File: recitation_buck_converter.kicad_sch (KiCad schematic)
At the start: 9 parts, among them U1 TPS54233

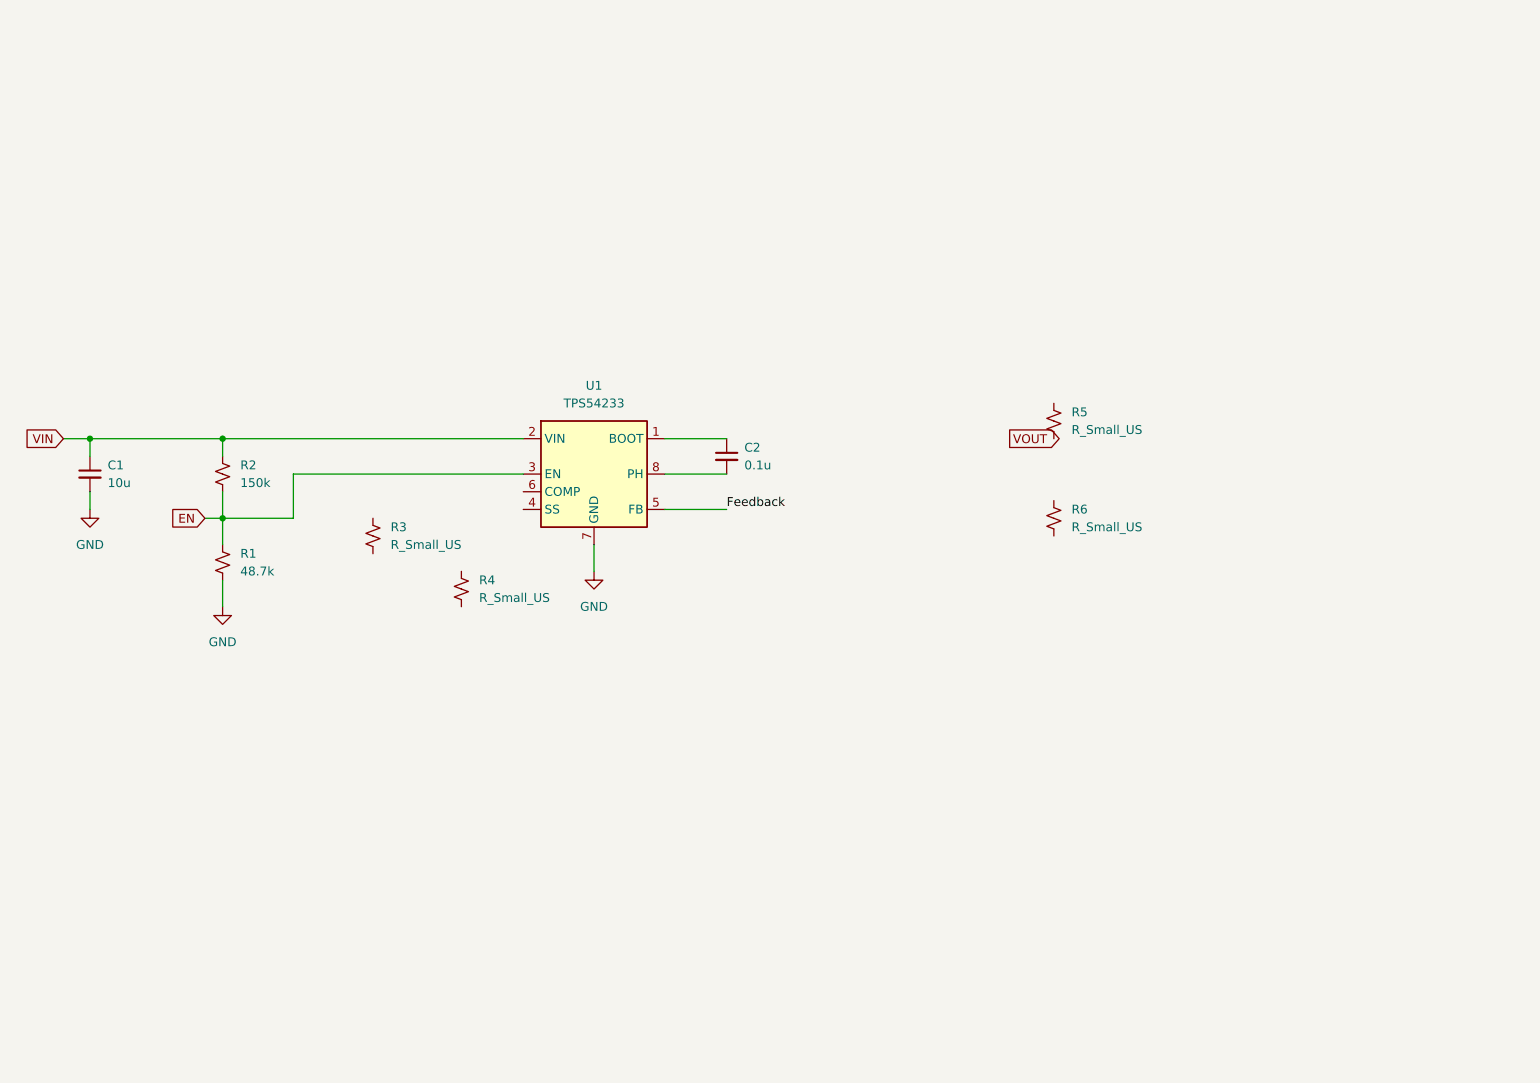
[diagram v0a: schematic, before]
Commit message: feat: update components to match specs and start layout
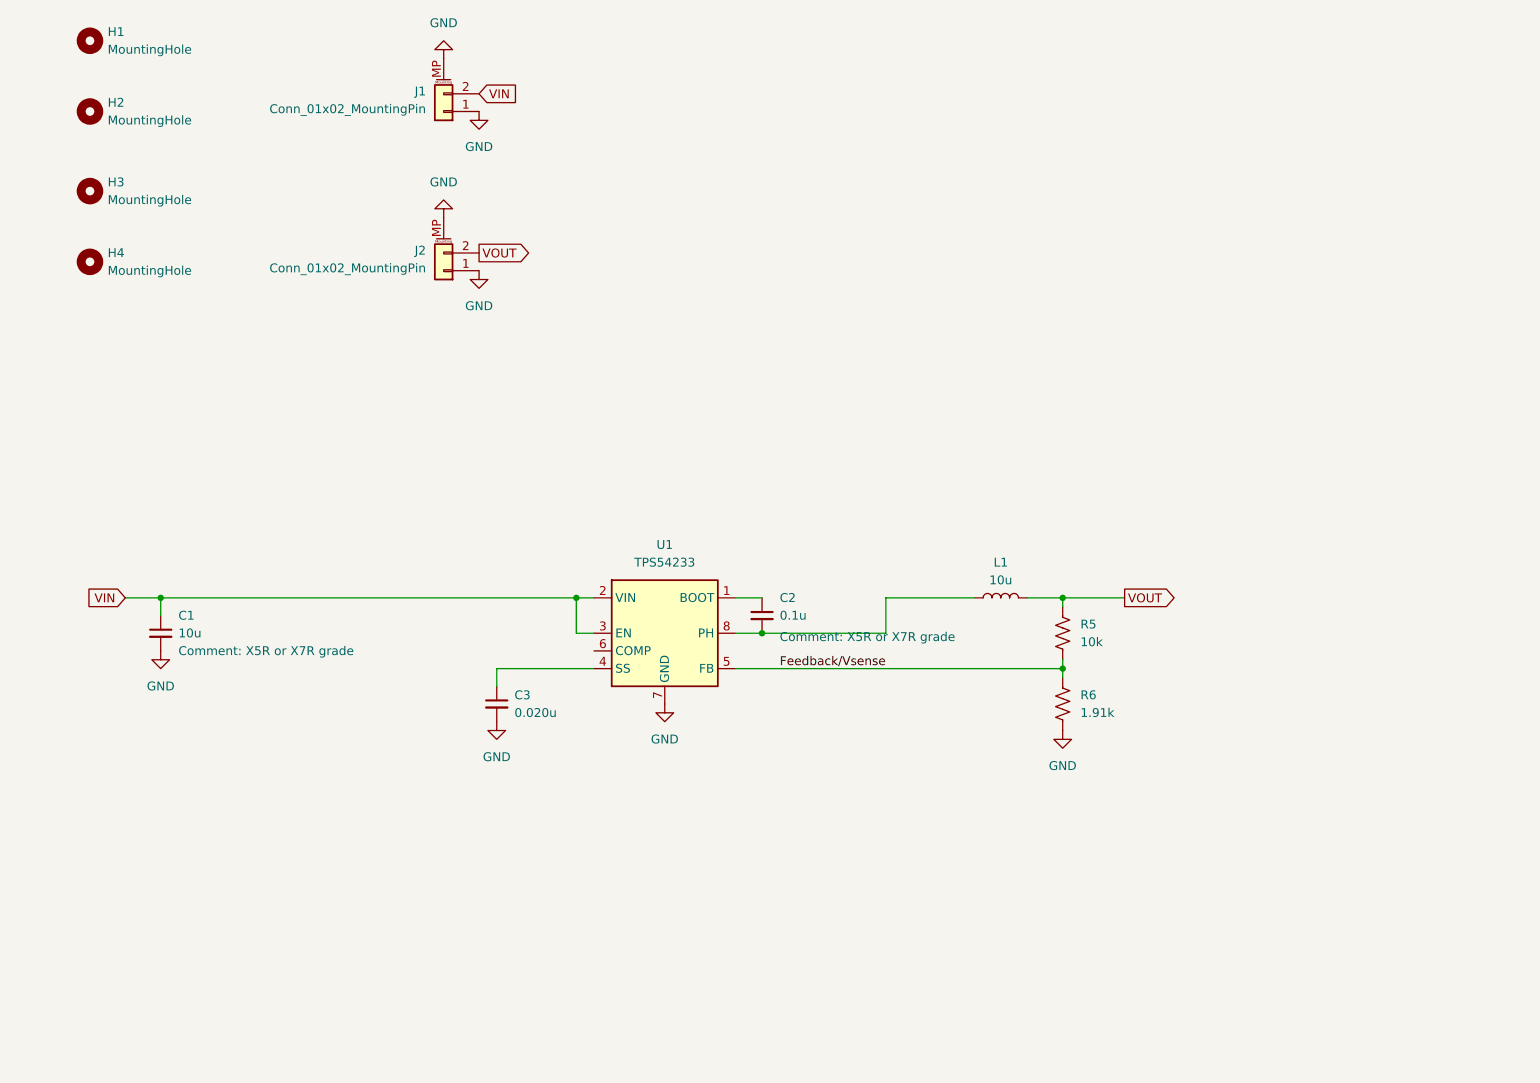
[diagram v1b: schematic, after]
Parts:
- removed R1: 48.7k, Resistor_SMD:R_0805_2012Metric_Pad1.20x1.40mm_HandSolder, symbol Device:R_Small_US
- removed R2: 150k, Resistor_SMD:R_0805_2012Metric_Pad1.20x1.40mm_HandSolder, symbol Device:R_Small_US
- removed R3, R4, R5, R6: R_Small_US, symbol Device:R_Small_US
- added C3: 0.020u, Capacitor_SMD:C_0805_2012Metric_Pad1.18x1.45mm_HandSolder, symbol Device:C_Small
- added H1, H2, H3, H4: MountingHole, MountingHole:MountingHole_2.2mm_M2, symbol Mechanical:MountingHole
- added J1, J2: Conn_01x02_MountingPin, Connector_JST:JST_XH_B2B-XH-AM_1x02_P2.50mm_Vertical, symbol Connector_Generic_MountingPin:Conn_01x02_MountingPin
- added L1: 10u, Inductor_THT:L_Axial_L9.5mm_D4.0mm_P5.08mm_Vertical_Fastron_SMCC, symbol Device:L
- added R5: 10k, Resistor_SMD:R_0805_2012Metric, symbol Device:R_US
- added R6: 1.91k, Resistor_SMD:R_0805_2012Metric, symbol Device:R_US
- C1: footprint Capacitor_SMD:C_0805_2012Metric_Pad1.18x1.45mm_HandSolder -> (none); Comment (none) -> X5R or X7R grade; Digikey PN 490-10500-1-ND -> (none)
- C2: Comment (none) -> X5R or X7R grade
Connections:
- net EN is gone; now on net VIN: U1.3 (EN)
- net GND: now also C3.2, J1.1 (Pin_1), J1.MP (MountPin), J2.1 (Pin_1), J2.MP (MountPin), R6.2
- net VIN: now also J1.2 (Pin_2)
- net VOUT: now also J2.2 (Pin_2), L1.2, R5.1
- net at U1.4 (SS): now also C3.1
- net at C2.2, U1.8 (PH): now also L1.1
- net Feedback renamed Feedback/Vsense
- net Feedback/Vsense: now also R5.2, R6.1
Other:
- moved on the sheet: C1, C2, U1

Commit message: feat: add output components, float EN, and layouu with good track width
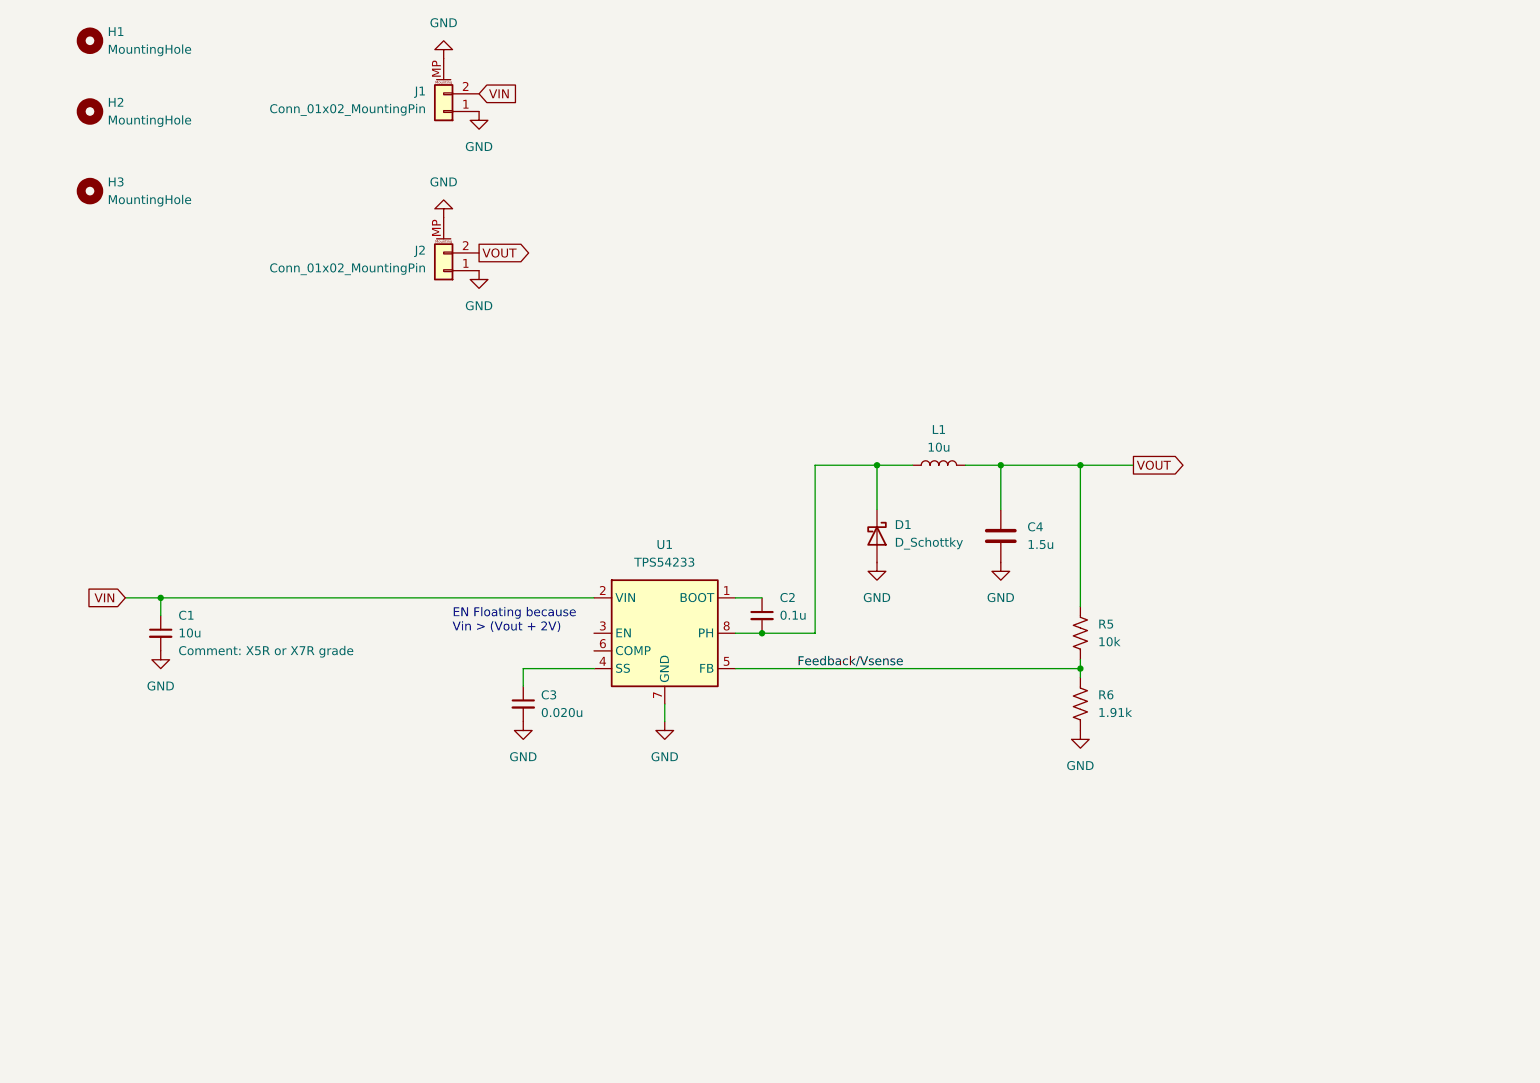
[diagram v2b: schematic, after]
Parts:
- removed H4: MountingHole, MountingHole:MountingHole_2.2mm_M2, symbol Mechanical:MountingHole
- added C4: 1.5u, Capacitor_SMD:C_0805_2012Metric_Pad1.18x1.45mm_HandSolder, symbol Device:C
- added D1: D_Schottky, ToshibaUS2H:US2H, symbol Device:D_Schottky
- C1: footprint (none) -> Capacitor_SMD:C_0805_2012Metric_Pad1.18x1.45mm_HandSolder; Digikey PN (none) -> 399-11939-2-ND
- R6: footprint Resistor_SMD:R_0805_2012Metric -> Resistor_SMD:R_0805_2012Metric_Pad1.20x1.40mm_HandSolder
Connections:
- net GND: now also C4.2, D1.2 (A)
- net VIN: no longer U1.3 (EN)
- net VOUT: now also C4.1
- net at C2.2, L1.1, U1.8 (PH): now also D1.1 (K)
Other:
- note added: "EN Floating because Vin > (Vout + 2V)"
- moved on the sheet: C3, L1, R5, R6

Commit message: feat: add compensation network; finish pcb
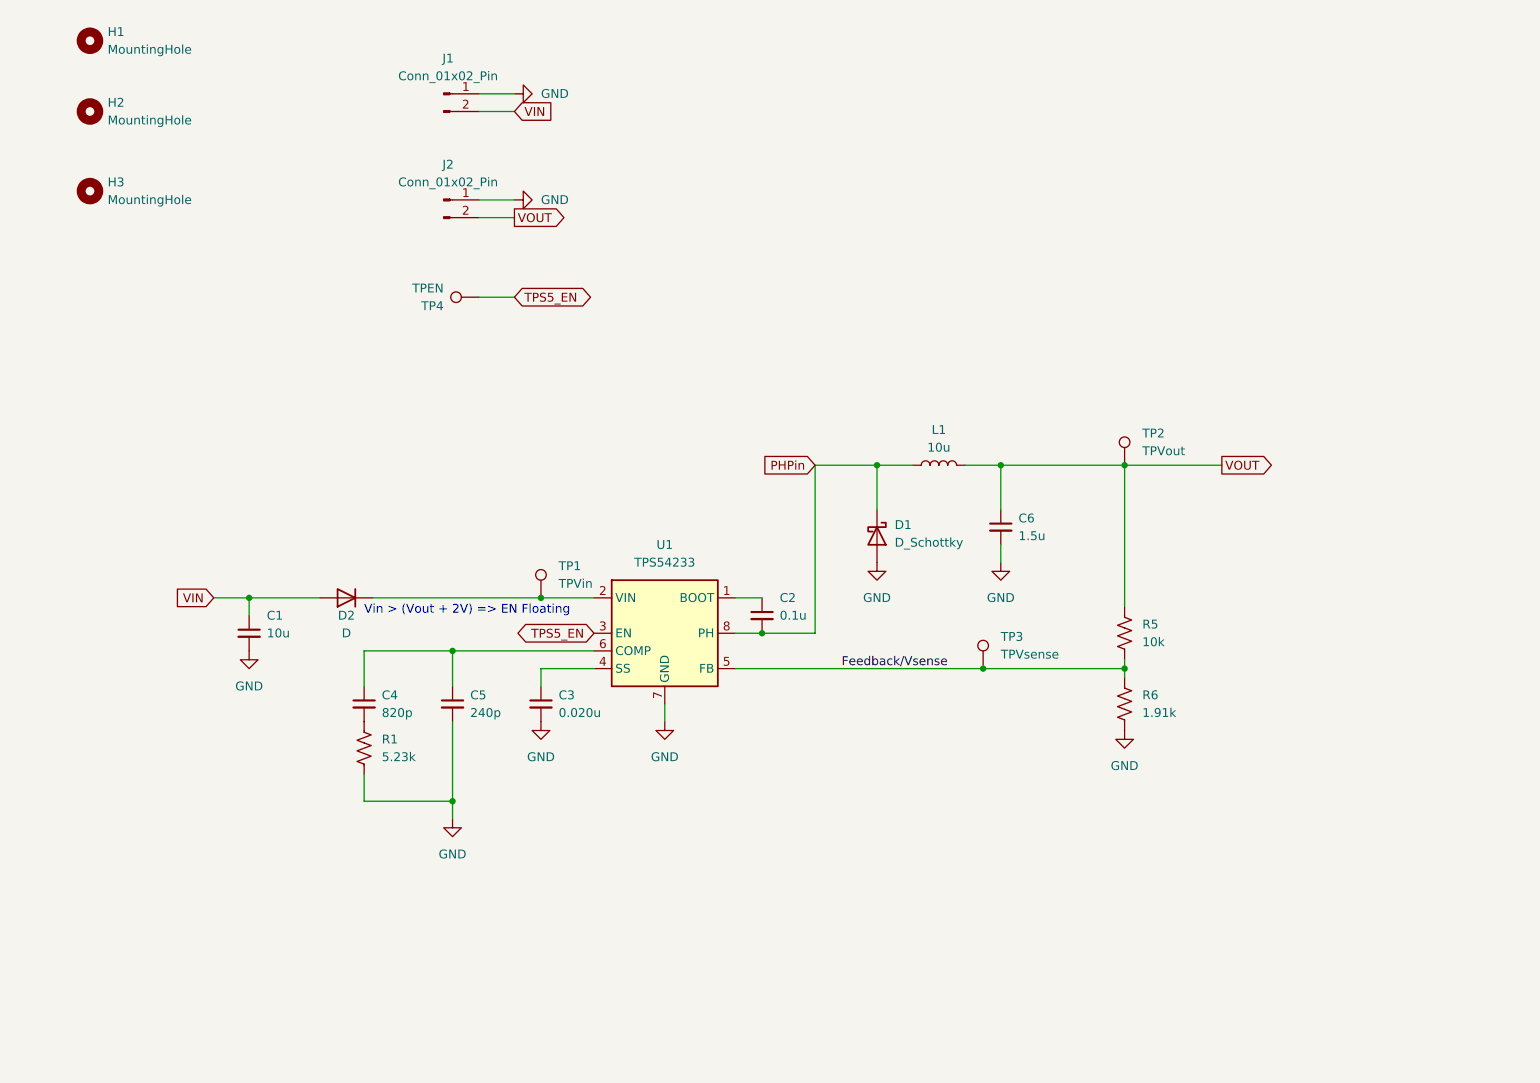
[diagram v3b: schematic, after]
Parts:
- removed C4: 1.5u, Capacitor_SMD:C_0805_2012Metric_Pad1.18x1.45mm_HandSolder, symbol Device:C
- removed J1, J2: Conn_01x02_MountingPin, Connector_JST:JST_XH_B2B-XH-AM_1x02_P2.50mm_Vertical, symbol Connector_Generic_MountingPin:Conn_01x02_MountingPin
- added C4: 820p, Capacitor_SMD:C_0805_2012Metric_Pad1.18x1.45mm_HandSolder, symbol Device:C_Small
- added C5: 240p, Capacitor_SMD:C_0805_2012Metric_Pad1.18x1.45mm_HandSolder, symbol Device:C_Small
- added C6: 1.5u, Capacitor_SMD:C_0805_2012Metric_Pad1.18x1.45mm_HandSolder, symbol Device:C_Small
- added D2: D, Diode_SMD:D_SMA, symbol Device:D
- added J1, J2: Conn_01x02_Pin, Connector_JST:JST_XH_B2B-XH-AM_1x02_P2.50mm_Vertical, symbol Connector:Conn_01x02_Pin
- added R1: 5.23k, Resistor_SMD:R_0805_2012Metric_Pad1.20x1.40mm_HandSolder, symbol Device:R_US
- added TP1: TPVin, TestPoint:TestPoint_Pad_1.5x1.5mm, symbol Connector:TestPoint
- added TP2: TPVout, TestPoint:TestPoint_Pad_1.5x1.5mm, symbol Connector:TestPoint
- added TP3: TPVsense, TestPoint:TestPoint_Pad_1.5x1.5mm, symbol Connector:TestPoint
- added TP4: TPEN, TestPoint:TestPoint_Pad_1.5x1.5mm, symbol Connector:TestPoint
- C1: Comment X5R or X7R grade -> (none)
- U1: Digikey PN 296-26985-5-ND -> 296-23902-1-ND
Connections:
- net Feedback/Vsense: now also TP3.1
- net GND: now also C5.2, C6.2, J1.1 (Pin_1), J2.1 (Pin_1), R1.2
- net VIN: now also D2.2 (A), J1.2 (Pin_2); no longer U1.2 (VIN)
- net VOUT: now also C6.1, J2.2 (Pin_2), TP2.1
- net TPS5_EN: now reaches U1.3 (EN)
- net TPS5_EN: now also TP4.1
- net at U1.6 (COMP): now also C4.1, C5.1
- net PHPin: now reaches C2.2, D1.1 (K), L1.1, U1.8 (PH)
- new net: C4.2, R1.1
- new net: D2.1 (K), TP1.1, U1.2 (VIN)
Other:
- note added: "Vin > (Vout + 2V) => EN Floating"
- note removed: "EN Floating because Vin > (Vout + 2V)"
- moved on the sheet: C1, C3, R5, R6

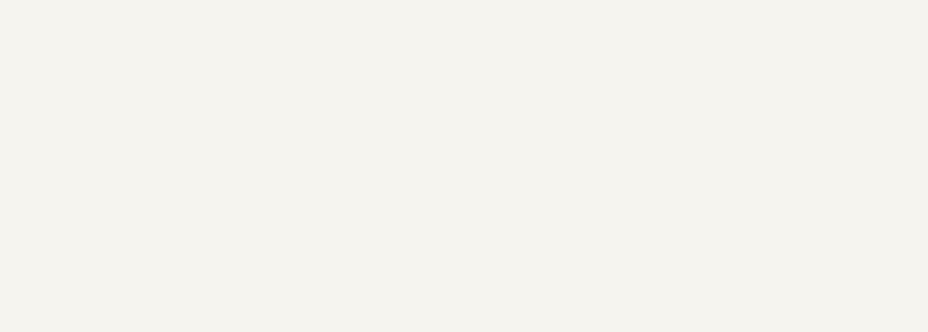
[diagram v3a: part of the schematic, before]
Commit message: fix(pcb): move dimensions to drawing layer
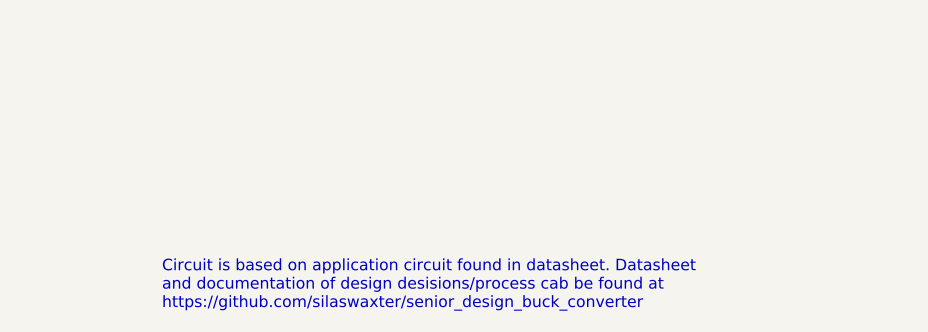
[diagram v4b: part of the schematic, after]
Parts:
- C2: Comment X5R or X7R grade -> (none)
- J1, J2: Digikey PN (none) -> DNP; DigikeyPN DNP -> (none)
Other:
- note added: "Circuit is based on application circuit found in datasheet. Datasheet and documentation of design desisions/process cab be found at https://github.com/silaswaxter/senior_design_buck_converter"
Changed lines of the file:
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@@
+    (effects (font (size 1.27 1.27)) (justify left bottom))
+  )
+  (text "Circuit is based on application circuit found in datasheet. Datasheet\nand documentation of design desisions/process cab be found at \nhttps://github.com/silaswaxter/senior_design_buck_converter"
+    (at 158.75 170.18 0)
     (effects (font (size 1.27 1.27)) (justify left bottom))
   )
@@
       (effects (font (size 1.27 1.27)) hide)
     )
-    (property "DigikeyPN" "DNP" (at 86.36 45.72 0)
+    (property "Digikey PN" "DNP" (at 86.36 45.72 0)
       (effects (font (size 1.27 1.27)) hide)
     )
@@
       (effects (font (size 1.27 1.27)) hide)
     )
-    (property "DigikeyPN" "DNP" (at 86.36 30.48 0)
+    (property "Digikey PN" "DNP" (at 86.36 30.48 0)
       (effects (font (size 1.27 1.27)) hide)
     )
@@
       (effects (font (size 1.27 1.27)) hide)
     )
-    (property "Comment" "X5R or X7R grade" (at 134.62 107.95 0) (show_name)
+    (property "Comment" "" (at 134.62 107.95 0) (show_name)
       (effects (font (size 1.27 1.27)) (justify left bottom) hide)
     )
